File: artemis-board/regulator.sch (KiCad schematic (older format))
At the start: 32 parts, among them Q5 AO3401A, Q6 AO3401A, Q7 2N7002, Q8 2N7002, Q9 AO3401A, U10 FP6291LR, U11 ME6210A33P, U12 ME6210A33P

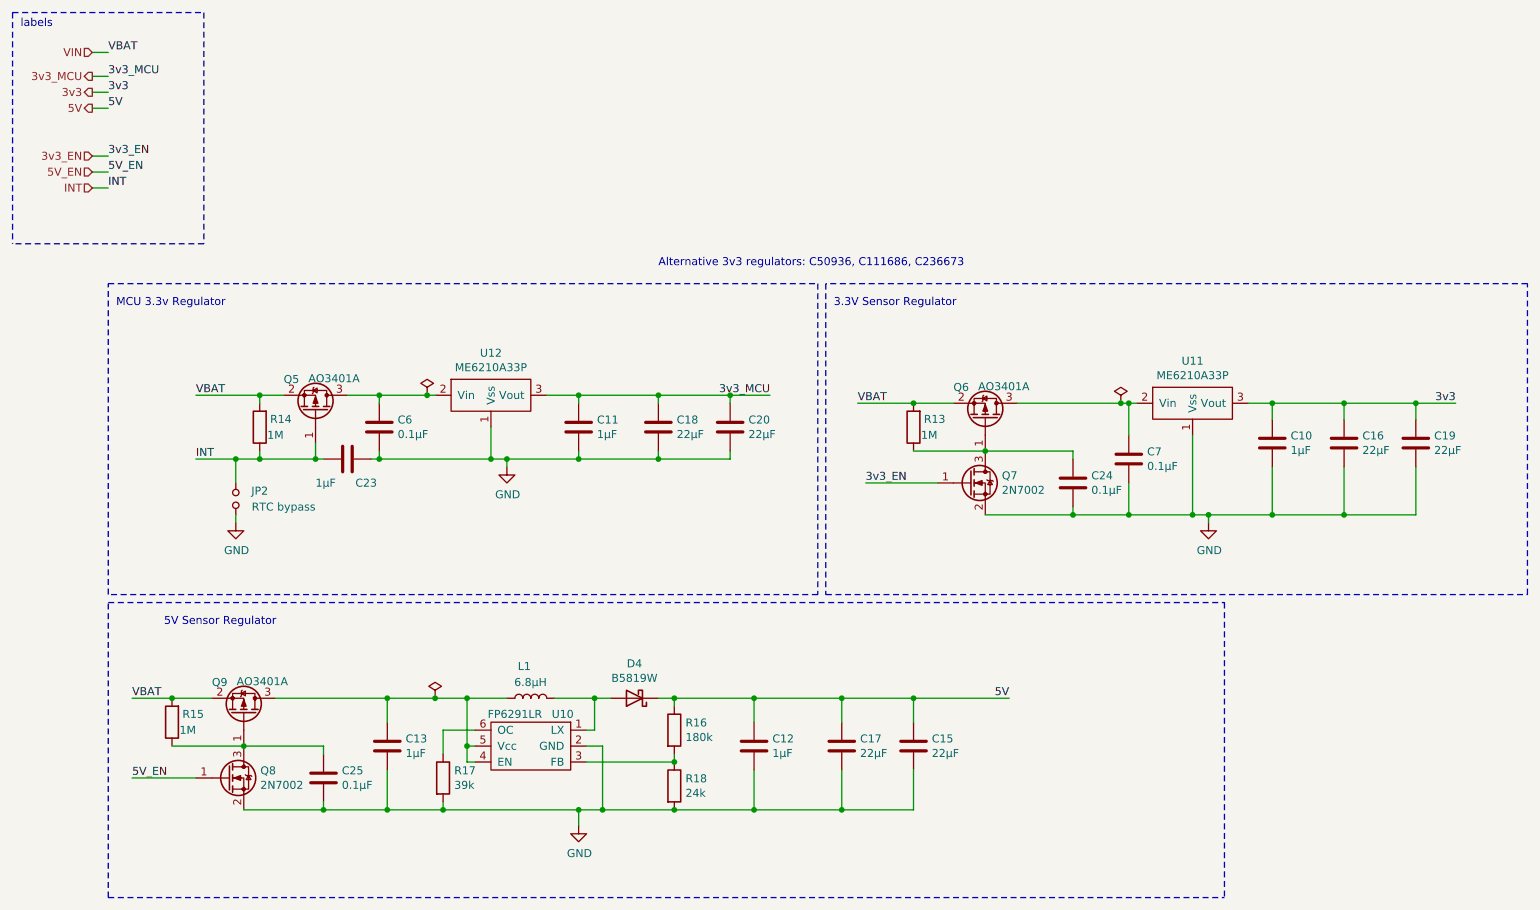
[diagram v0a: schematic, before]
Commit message: added comments and swapped polarity of Vin connector
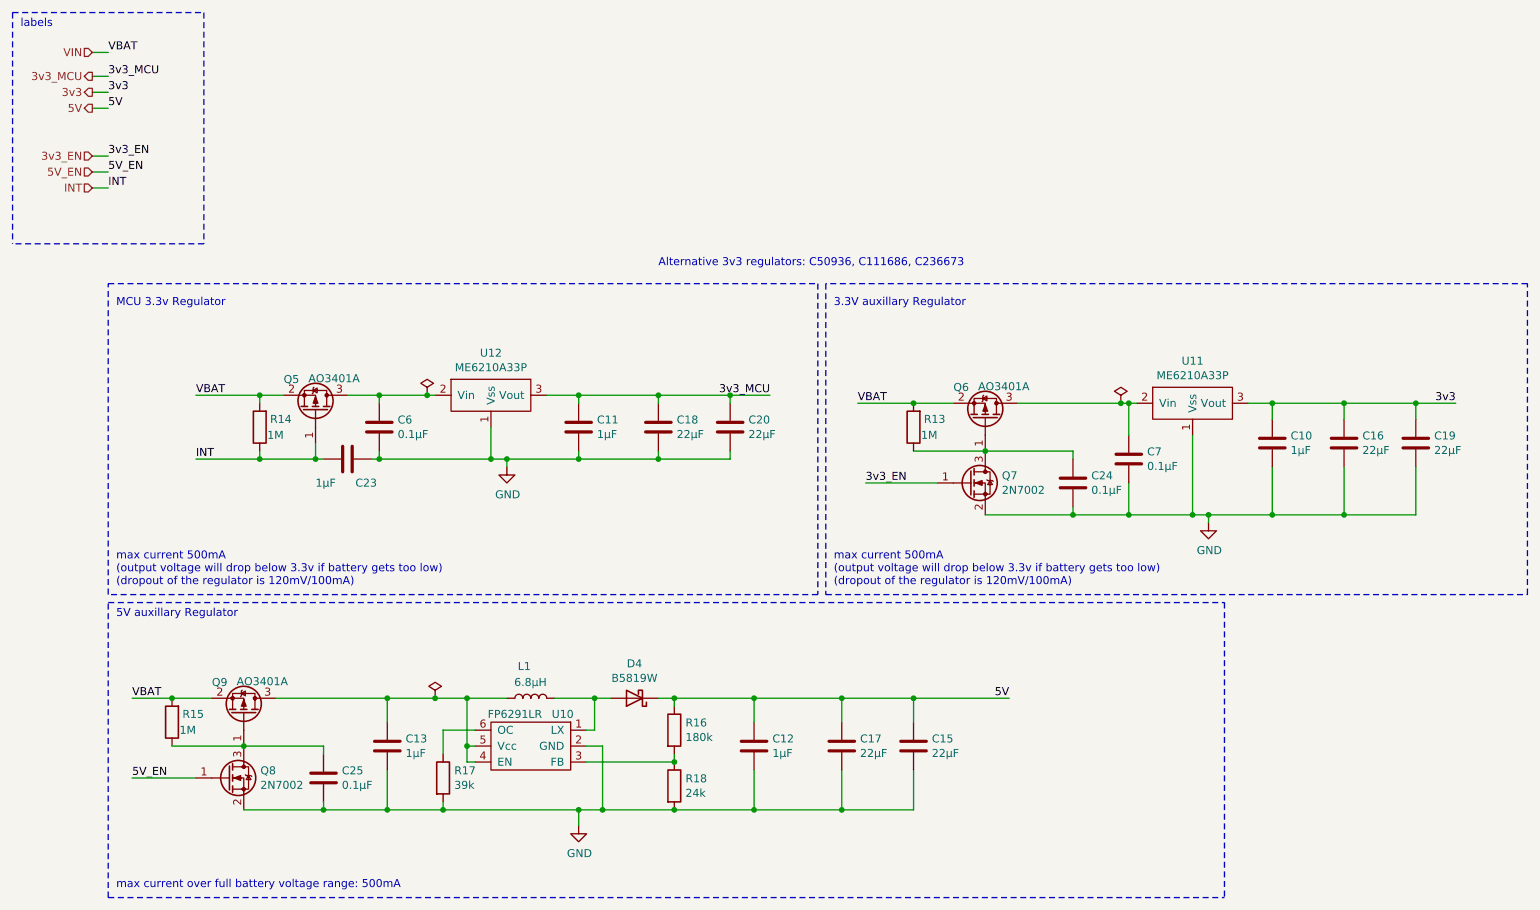
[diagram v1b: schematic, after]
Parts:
- removed JP2: RTC bypass, Connector_PinHeader_2.54mm:PinHeader_1x02_P2.54mm_Vertical, symbol Device:Jumper_NO_Small
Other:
- note added: "3.3V auxillary Regulator\n"
- note added: "5V auxillary Regulator"
- note added: "max current 500mA\n(output voltage will drop below 3.3v if battery gets too low)\n(dropout of the regulator is 120mV/100mA)"
- note added: "max current over full battery voltage range: 500mA"
- note removed: "3.3V Sensor Regulator\n"
- note removed: "5V Sensor Regulator"
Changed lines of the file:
@@
 	10100 2300 5700 2300
 Text Notes 5750 2450 0    50   ~ 0
-3.3V Sensor Regulator\n
+3.3V auxillary Regulator\n
 Wire Notes Line
 	8200 4300 8200 6150
 Wire Notes Line
 	1200 6150 1200 4300
-Text Notes 1550 4450 0    50   ~ 0
-5V Sensor Regulator
+Text Notes 1250 4400 0    50   ~ 0
+5V auxillary Regulator
 Text HLabel 1100 1700 0    50   Input ~ 0
 INT
@@
 Connection ~ 3600 3400
 Wire Wire Line
-	1750 3400 2000 3400
-Wire Wire Line
 	2150 3400 2150 3350
 Connection ~ 2150 3400
@@
 Wire Wire Line
 	2900 3000 3200 3000
-Connection ~ 2000 3400
-Wire Wire Line
-	2000 3400 2150 3400
 Wire Wire Line
 	3600 3400 3700 3400
@@
 Wire Wire Line
 	8100 3750 8500 3750
-Wire Wire Line
-	2000 3400 2000 3550
-$Comp
-L power:GND #PWR0132
-U 1 1 600F44E8
-P 2000 3800
-F 0 "#PWR0132" H 2000 3550 50  0001 C CNN
-F 1 "GND" H 2005 3627 50  0000 C CNN
-F 2 "" H 2000 3800 50  0001 C CNN
-F 3 "" H 2000 3800 50  0001 C CNN
-	1    2000 3800
-	1    0    0    -1
-$EndComp
-Wire Wire Line
-	2000 3800 2000 3750
 Wire Notes Line
 	1800 600  1800 2050
@@
 	1    9400 3300
 	1    0    0    -1
-$EndComp
-$Comp
-L Device:Jumper_NO_Small JP2
-U 1 1 600C2DE8
-P 2000 3650
-F 0 "JP2" V 2050 3500 50  0000 C CNN
-F 1 "RTC bypass" V 1950 3350 50  0000 C CNN
-F 2 "Connector_PinHeader_2.54mm:PinHeader_1x02_P2.54mm_Vertical" H 2000 3650 50  0001 C CNN
-F 3 "~" H 2000 3650 50  0001 C CNN
-	1    2000 3650
-	0    -1   -1   0
 $EndComp
 $Comp
@@
 Wire Wire Line
 	4000 4900 4250 4900
+Text Notes 1250 6100 0    50   ~ 0
+max current over full battery voltage range: 500mA
+Text Notes 5750 4200 0    50   ~ 0
+max current 500mA\n(output voltage will drop below 3.3v if battery gets too low)\n(dropout of the regulator is 120mV/100mA)
+Text Notes 1250 4200 0    50   ~ 0
+max current 500mA\n(output voltage will drop below 3.3v if battery gets too low)\n(dropout of the regulator is 120mV/100mA)
+Wire Wire Line
+	1750 3400 2150 3400
 $EndSCHEMATC

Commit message: swapped and added some lcsc part numbers and DNP markers
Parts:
- C10, C11, C12, C13, C23: footprint Capacitor_SMD:C_0603_1608Metric_Pad1.05x0.95mm_HandSolder -> Capacitor_SMD:C_0603_1608Metric_Pad1.08x0.95mm_HandSolder
- D4: LCSC C8598 -> C8598
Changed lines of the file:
@@
 F 0 "C13" H 3065 5246 50  0000 L CNN
 F 1 "1µF" H 3065 5155 50  0000 L CNN
-F 2 "Capacitor_SMD:C_0603_1608Metric_Pad1.05x0.95mm_HandSolder" H 2988 5050 50  0001 C CNN
+F 2 "Capacitor_SMD:C_0603_1608Metric_Pad1.08x0.95mm_HandSolder" H 2988 5050 50  0001 C CNN
 F 3 "~" H 2950 5200 50  0001 C CNN
 F 4 "C15849" H 2950 5200 50  0001 C CNN "LCSC"
@@
 F 0 "C12" H 5365 5246 50  0000 L CNN
 F 1 "1µF" H 5365 5155 50  0000 L CNN
-F 2 "Capacitor_SMD:C_0603_1608Metric_Pad1.05x0.95mm_HandSolder" H 5288 5050 50  0001 C CNN
+F 2 "Capacitor_SMD:C_0603_1608Metric_Pad1.08x0.95mm_HandSolder" H 5288 5050 50  0001 C CNN
 F 3 "~" H 5250 5200 50  0001 C CNN
 F 4 "C15849" H 5250 5200 50  0001 C CNN "LCSC"
@@
 F 2 "Diode_SMD:D_SOD-123" H 4500 4900 50  0001 C CNN
 F 3 "https://datasheet.lcsc.com/szlcsc/Changjiang-Electronics-Tech-CJ-B5819W_C8598.pdf" H 4500 4900 50  0001 C CNN
-F 4 " C8598" H 4500 4900 50  0001 C CNN "LCSC"
+F 4 "C8598" H 4500 4900 50  0001 C CNN "LCSC"
 	1    4500 4900
 	-1   0    0    1
@@
 F 0 "C23" V 2850 3450 50  0000 L CNN
 F 1 "1µF" V 2850 3200 50  0000 L CNN
-F 2 "Capacitor_SMD:C_0603_1608Metric_Pad1.05x0.95mm_HandSolder" H 2738 3250 50  0001 C CNN
+F 2 "Capacitor_SMD:C_0603_1608Metric_Pad1.08x0.95mm_HandSolder" H 2738 3250 50  0001 C CNN
 F 3 "~" H 2700 3400 50  0001 C CNN
 F 4 "C15849" H 2700 3400 50  0001 C CNN "LCSC"
@@
 F 0 "C11" H 4265 3246 50  0000 L CNN
 F 1 "1µF" H 4265 3155 50  0000 L CNN
-F 2 "Capacitor_SMD:C_0603_1608Metric_Pad1.05x0.95mm_HandSolder" H 4188 3050 50  0001 C CNN
+F 2 "Capacitor_SMD:C_0603_1608Metric_Pad1.08x0.95mm_HandSolder" H 4188 3050 50  0001 C CNN
 F 3 "~" H 4150 3200 50  0001 C CNN
 F 4 "C15849" H 4150 3200 50  0001 C CNN "LCSC"
@@
 F 0 "C10" H 8615 3346 50  0000 L CNN
 F 1 "1µF" H 8615 3255 50  0000 L CNN
-F 2 "Capacitor_SMD:C_0603_1608Metric_Pad1.05x0.95mm_HandSolder" H 8538 3150 50  0001 C CNN
+F 2 "Capacitor_SMD:C_0603_1608Metric_Pad1.08x0.95mm_HandSolder" H 8538 3150 50  0001 C CNN
 F 3 "~" H 8500 3300 50  0001 C CNN
 F 4 "C15849" H 8500 3300 50  0001 C CNN "LCSC"

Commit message: added jumpers for use without io expander
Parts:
- added R24, R25: 1M, Resistor_SMD:R_0603_1608Metric_Pad1.05x0.95mm_HandSolder, symbol Device:R
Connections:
- net 3v3_EN: now also R24.1
- net 5V_EN: now also R25.1
- net GND: now also R24.2, R25.2
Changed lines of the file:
@@
 	8950 3050 9400 3050
 Wire Wire Line
-	5950 3550 6400 3550
+	5950 3550 6300 3550
 Wire Notes Line
 	600  600  1800 600
@@
 	1600 5200 2050 5200
 Wire Wire Line
-	1350 5400 1750 5400
+	1350 5400 1650 5400
 Wire Wire Line
 	2950 5600 3300 5600
@@
 Wire Wire Line
 	1750 3400 2150 3400
+$Comp
+L Device:R R?
+U 1 1 60D6827B
+P 6500 3750
+AR Path="/5F639F48/60D6827B" Ref="R?"  Part="1"
+AR Path="/5F63A0E9/60D6827B" Ref="R24"  Part="1"
+F 0 "R24" V 6400 3600 50  0000 L CNN
+F 1 "1M" V 6400 3800 50  0000 L CNN
+F 2 "Resistor_SMD:R_0603_1608Metric_Pad1.05x0.95mm_HandSolder" V 6430 3750 50  0001 C CNN
+F 3 "~" H 6500 3750 50  0001 C CNN
+F 4 "C22935" H 6500 3750 50  0001 C CNN "LCSC"
+	1    6500 3750
+	0    -1   -1   0
+$EndComp
+$Comp
+L Device:R R?
+U 1 1 60D6B03E
+P 1850 5600
+AR Path="/5F639F48/60D6B03E" Ref="R?"  Part="1"
+AR Path="/5F63A0E9/60D6B03E" Ref="R25"  Part="1"
+F 0 "R25" V 1750 5450 50  0000 L CNN
+F 1 "1M" V 1750 5650 50  0000 L CNN
+F 2 "Resistor_SMD:R_0603_1608Metric_Pad1.05x0.95mm_HandSolder" V 1780 5600 50  0001 C CNN
+F 3 "~" H 1850 5600 50  0001 C CNN
+F 4 "C22935" H 1850 5600 50  0001 C CNN "LCSC"
+	1    1850 5600
+	0    -1   -1   0
+$EndComp
+Wire Wire Line
+	2000 5600 2050 5600
+Connection ~ 2050 5600
+Wire Wire Line
+	1700 5600 1650 5600
+Wire Wire Line
+	1650 5600 1650 5400
+Connection ~ 1650 5400
+Wire Wire Line
+	1650 5400 1750 5400
+Wire Wire Line
+	6350 3750 6300 3750
+Wire Wire Line
+	6300 3750 6300 3550
+Connection ~ 6300 3550
+Wire Wire Line
+	6300 3550 6400 3550
+Wire Wire Line
+	6650 3750 6700 3750
+Connection ~ 6700 3750
 $EndSCHEMATC

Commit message: connected VccP of io expander back to 3v3, changed some footprint
also added NMos so voltage divider can be used
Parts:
- Q5, Q6, Q9: footprint Package_TO_SOT_SMD:SOT-23_Handsoldering -> Package_TO_SOT_SMD:SOT-23
- R13, R14, R15, R24, R25: footprint Resistor_SMD:R_0603_1608Metric_Pad1.05x0.95mm_HandSolder -> Resistor_SMD:R_0603_1608Metric_Pad0.98x0.95mm_HandSolder
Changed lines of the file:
@@
 F 0 "Q9" V 2250 4800 50  0000 L CNN
 F 1 "AO3401A" V 2255 4955 50  0000 L CNN
-F 2 "Package_TO_SOT_SMD:SOT-23_Handsoldering" H 2250 4925 50  0001 L CIN
+F 2 "Package_TO_SOT_SMD:SOT-23" H 2250 4925 50  0001 L CIN
 F 3 "http://www.aosmd.com/pdfs/datasheet/AO3401A.pdf" H 2050 5000 50  0001 L CNN
 F 4 "C15127" H 2050 5000 50  0001 C CNN "LCSC"
@@
 F 0 "R13" H 6050 3150 50  0000 L CNN
 F 1 "1M" H 6100 3250 50  0000 L CNN
-F 2 "Resistor_SMD:R_0603_1608Metric_Pad1.05x0.95mm_HandSolder" V 6180 3200 50  0001 C CNN
+F 2 "Resistor_SMD:R_0603_1608Metric_Pad0.98x0.95mm_HandSolder" V 6180 3200 50  0001 C CNN
 F 3 "~" H 6250 3200 50  0001 C CNN
 F 4 "C22935" H 6250 3200 50  0001 C CNN "LCSC"
@@
 F 0 "R14" H 1950 3150 50  0000 L CNN
 F 1 "1M" H 2000 3250 50  0000 L CNN
-F 2 "Resistor_SMD:R_0603_1608Metric_Pad1.05x0.95mm_HandSolder" V 2080 3200 50  0001 C CNN
+F 2 "Resistor_SMD:R_0603_1608Metric_Pad0.98x0.95mm_HandSolder" V 2080 3200 50  0001 C CNN
 F 3 "~" H 2150 3200 50  0001 C CNN
 F 4 "C22935" H 2150 3200 50  0001 C CNN "LCSC"
@@
 F 0 "Q6" V 6900 2950 50  0000 L CNN
 F 1 "AO3401A" V 6905 3105 50  0000 L CNN
-F 2 "Package_TO_SOT_SMD:SOT-23_Handsoldering" H 6900 3075 50  0001 L CIN
+F 2 "Package_TO_SOT_SMD:SOT-23" H 6900 3075 50  0001 L CIN
 F 3 "http://www.aosmd.com/pdfs/datasheet/AO3401A.pdf" H 6700 3150 50  0001 L CNN
 F 4 "C15127" H 6700 3150 50  0001 C CNN "LCSC"
@@
 F 0 "Q5" V 2700 2900 50  0000 L CNN
 F 1 "AO3401A" V 2705 3055 50  0000 L CNN
-F 2 "Package_TO_SOT_SMD:SOT-23_Handsoldering" H 2700 3025 50  0001 L CIN
+F 2 "Package_TO_SOT_SMD:SOT-23" H 2700 3025 50  0001 L CIN
 F 3 "http://www.aosmd.com/pdfs/datasheet/AO3401A.pdf" H 2500 3100 50  0001 L CNN
 F 4 "C15127" H 2500 3100 50  0001 C CNN "LCSC"
@@
 F 0 "R15" H 1400 5000 50  0000 L CNN
 F 1 "1M" H 1450 5100 50  0000 L CNN
-F 2 "Resistor_SMD:R_0603_1608Metric_Pad1.05x0.95mm_HandSolder" V 1530 5050 50  0001 C CNN
+F 2 "Resistor_SMD:R_0603_1608Metric_Pad0.98x0.95mm_HandSolder" V 1530 5050 50  0001 C CNN
 F 3 "~" H 1600 5050 50  0001 C CNN
 F 4 "C22935" H 1600 5050 50  0001 C CNN "LCSC"
@@
 F 0 "R24" V 6400 3600 50  0000 L CNN
 F 1 "1M" V 6400 3800 50  0000 L CNN
-F 2 "Resistor_SMD:R_0603_1608Metric_Pad1.05x0.95mm_HandSolder" V 6430 3750 50  0001 C CNN
+F 2 "Resistor_SMD:R_0603_1608Metric_Pad0.98x0.95mm_HandSolder" V 6430 3750 50  0001 C CNN
 F 3 "~" H 6500 3750 50  0001 C CNN
 F 4 "C22935" H 6500 3750 50  0001 C CNN "LCSC"
@@
 F 0 "R25" V 1750 5450 50  0000 L CNN
 F 1 "1M" V 1750 5650 50  0000 L CNN
-F 2 "Resistor_SMD:R_0603_1608Metric_Pad1.05x0.95mm_HandSolder" V 1780 5600 50  0001 C CNN
+F 2 "Resistor_SMD:R_0603_1608Metric_Pad0.98x0.95mm_HandSolder" V 1780 5600 50  0001 C CNN
 F 3 "~" H 1850 5600 50  0001 C CNN
 F 4 "C22935" H 1850 5600 50  0001 C CNN "LCSC"
